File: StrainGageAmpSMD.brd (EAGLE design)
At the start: 47 x 49.5 mm, 55 parts

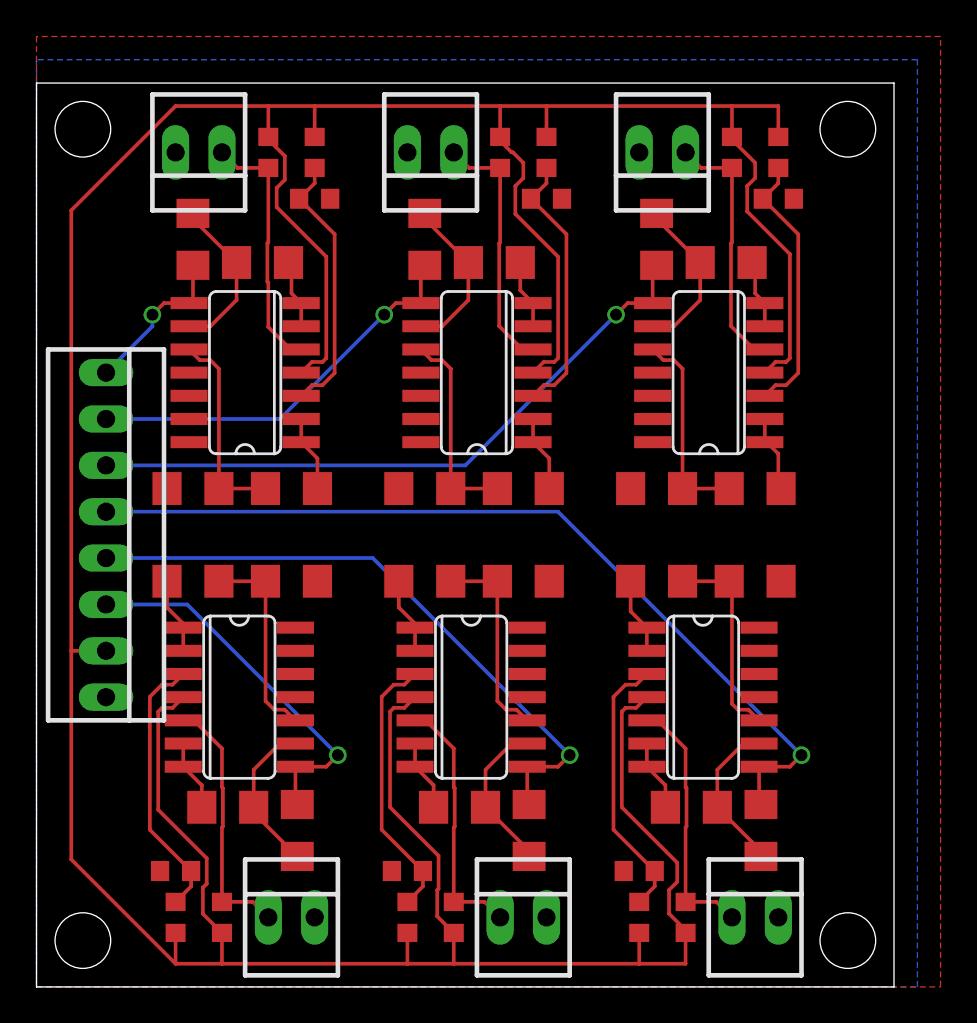
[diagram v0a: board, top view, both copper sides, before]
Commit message: Reduced from 6 channels to 3
-Reduced 6 channels to 3
-Changed all resistors to 0603 format
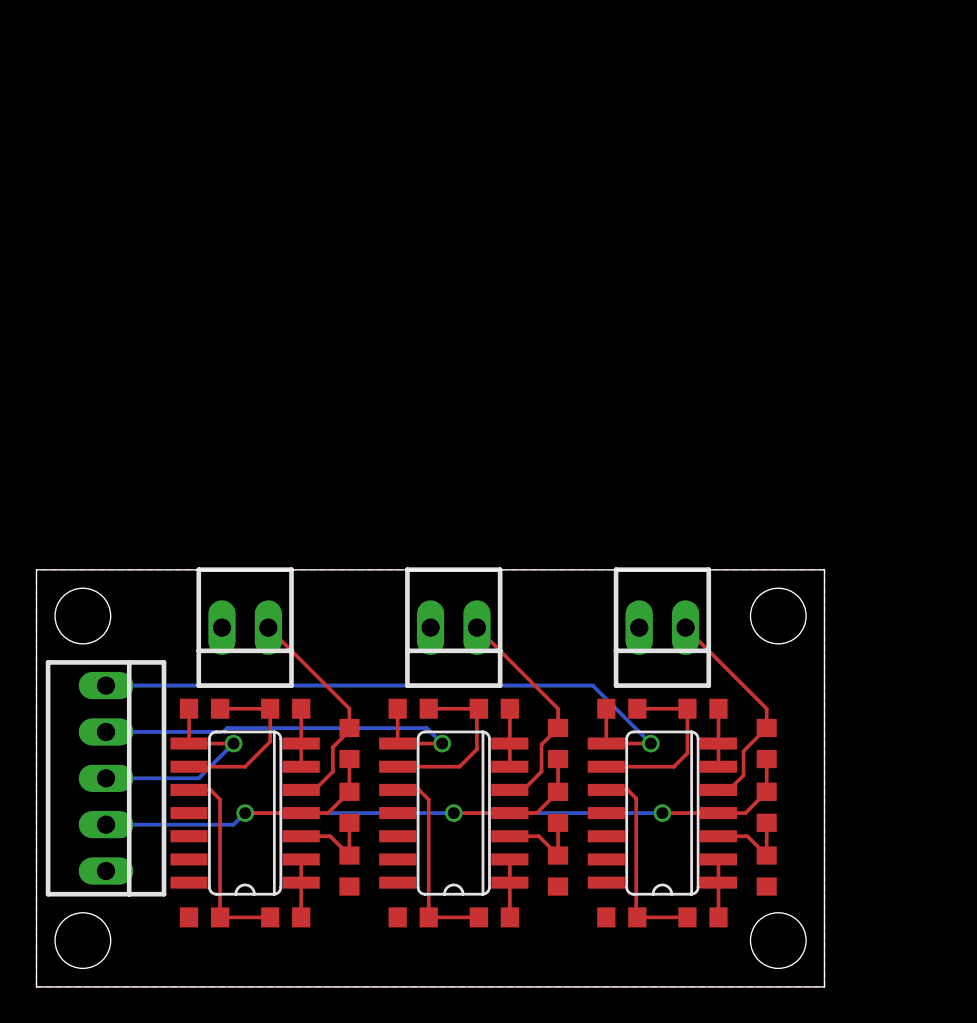
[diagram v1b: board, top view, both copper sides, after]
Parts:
- removed LM1, LM2, LM324: QUAD_OPAMPD, adafruit:SO14
- removed O0, O1, O2: 22-23-2021, con-molex:22-23-2021
- removed R10, R11, R17, R18, R4, R5: 2.2k, adafruit:R1206
- removed R12, R13, R14, R19, R20, R21, R6, R7, R8: 352, adafruit:R0603
- removed R15, R16, R2, R22, R3, R9: 560k, adafruit:R1206
- removed RTANGLE: 22-23-2081, con-molex:22-23-2081
- added GND_VCC_0_1_2: 22-23-2051, con-molex:22-23-2051
- R1: device adafruit:R1206 -> rcl:R0603
- R23, R24, R25, R29, R30, R31, R32, R36, R37, R38, R39: device adafruit:R1206 -> adafruit:R0603
- moved R40 36.9 mm to (18.4, 7.62), turned to 90 degrees
- moved R26 36.8 mm to (41.3, 7.62), turned to 90 degrees
- moved R33 36.8 mm to (29.8, 7.62), turned to 90 degrees
- moved R41 35.9 mm to (18.4, 11.1)
- moved R27 35.9 mm to (41.3, 11.1)
- moved R34 35.9 mm to (29.8, 11.1)
- moved R42 32.7 mm to (18.4, 14.6), turned to 270 degrees
- moved R35 32.5 mm to (29.8, 14.6), turned to 270 degrees
- moved R28 32.4 mm to (41.3, 14.6), turned to 270 degrees
- moved O3 26.2 mm to (12.7, 21.0)
- moved O4 26.1 mm to (24.1, 21.0)
- moved O5 26.0 mm to (35.6, 21.0)
- moved R23 25.8 mm to (33.3, 16.5), turned to 180 degrees
- moved R30 25.7 mm to (21.9, 16.5), turned to 180 degrees
- moved R37 25.7 mm to (10.5, 16.5), turned to 180 degrees
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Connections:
- removed net N$1: LM1.3, R12.2, R13.1
- removed net N$10: LM1.5, O1.1, R14.1
- removed net N$11: LM1.1, LM1.2, R10.1
- removed net N$12: LM1.6, LM1.7, R11.1
- removed net N$13: LM1.9, R11.2, R9.1
- removed net N$14: LM1.10, R1.1, R10.2
- removed net N$15: LM2.3, R19.2, R20.1
- removed net N$16: LM2.5, O2.1, R21.1
- removed net N$17: LM2.1, LM2.2, R17.1
- removed net N$18: LM2.6, LM2.7, R18.1
- removed net N$19: LM2.9, R16.1, R18.2
- removed net N$2: LM324.3, R6.2, R7.1
- removed net N$20: LM2.10, R15.1, R17.2
- removed net N$3: LM324.5, O0.1, R8.1
- removed net N$4: LM324.1, LM324.2, R4.1
- removed net N$5: LM324.6, LM324.7, R5.1
- removed net N$6: LM324.9, R3.1, R5.2
- removed net N$7: LM324.10, R2.1, R4.2
- removed net N$8: LM324.8, R3.2, RTANGLE.6
- removed net N$81: LM1.8, R9.2, RTANGLE.5
- removed net N$82: LM2.8, R16.2, RTANGLE.4
- net GND: now also GND_VCC_0_1_2.5; no longer LM1.11, LM2.11, LM324.11, O0.2, O1.2, O2.2, R12.1, R15.2, R19.1, R2.2, R22.2, R6.1, RTANGLE.8
- net N$26: now also R1.1; no longer R22.1
- net N$83: now also GND_VCC_0_1_2.1; no longer RTANGLE.3
- net N$84: now also GND_VCC_0_1_2.2; no longer RTANGLE.2
- net N$85: now also GND_VCC_0_1_2.3; no longer RTANGLE.1
- net VCC: now also GND_VCC_0_1_2.4; no longer LM1.4, LM2.4, LM324.4, R13.2, R14.2, R20.2, R21.2, R7.2, R8.2, RTANGLE.7
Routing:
- net VCC: track 228.2 -> 55.3 mm, vias 0 -> 3
- net N$82: track 48.3 -> 0.00 mm, vias 1 -> 0
- net N$81: track 34.6 -> 0.00 mm, vias 1 -> 0
- net N$8: track 20.8 -> 0.00 mm, vias 1 -> 0
- net N$1: track 14.9 -> 0.00 mm
- net N$15: track 14.9 -> 0.00 mm
- net N$2: track 14.9 -> 0.00 mm
- net N$16: track 14.1 -> 0.00 mm
- net N$10: track 14.1 -> 0.00 mm
- net N$3: track 14.1 -> 0.00 mm
- net N$20: track 11.2 -> 0.00 mm
- net N$7: track 11.2 -> 0.00 mm
- net N$14: track 11.2 -> 0.00 mm
- net N$33: track 14.7 -> 4.87 mm
- net N$21: track 14.7 -> 4.87 mm
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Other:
- board size 47 x 49.5 mm -> 43.2 x 22.9 mm
- board text added: "3Amp v0 Szczecinski 2020"
- board text added: "VCC"
- board text removed: "3"
- board text removed: "4"
- board text removed: "5"
- board text removed: "6Amp v1.1 Szczecinski 2018"
